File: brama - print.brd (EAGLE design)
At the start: 127.5 x 209.5 mm, 125 parts, among them IC1 AT90USB162A, IC3 AT90USB162A, J1 AVR_SPI_PRG_6OFFSET_PADS, J2 AVR_SPI_PRG_6OFFSET_PADS

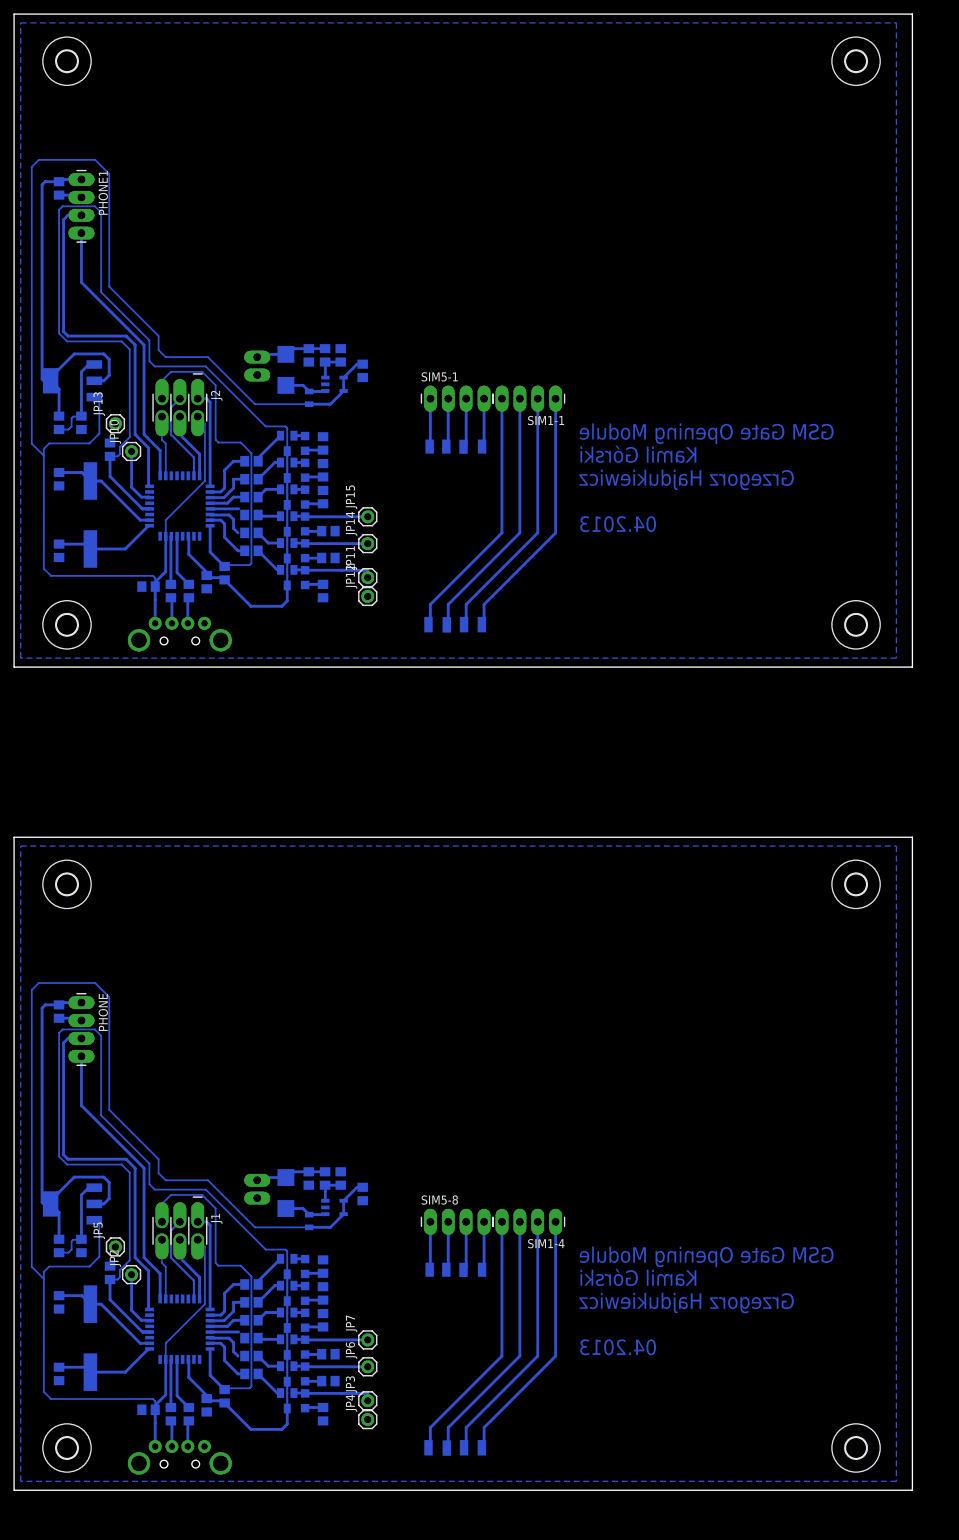
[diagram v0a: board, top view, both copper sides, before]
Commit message: L7805 Added
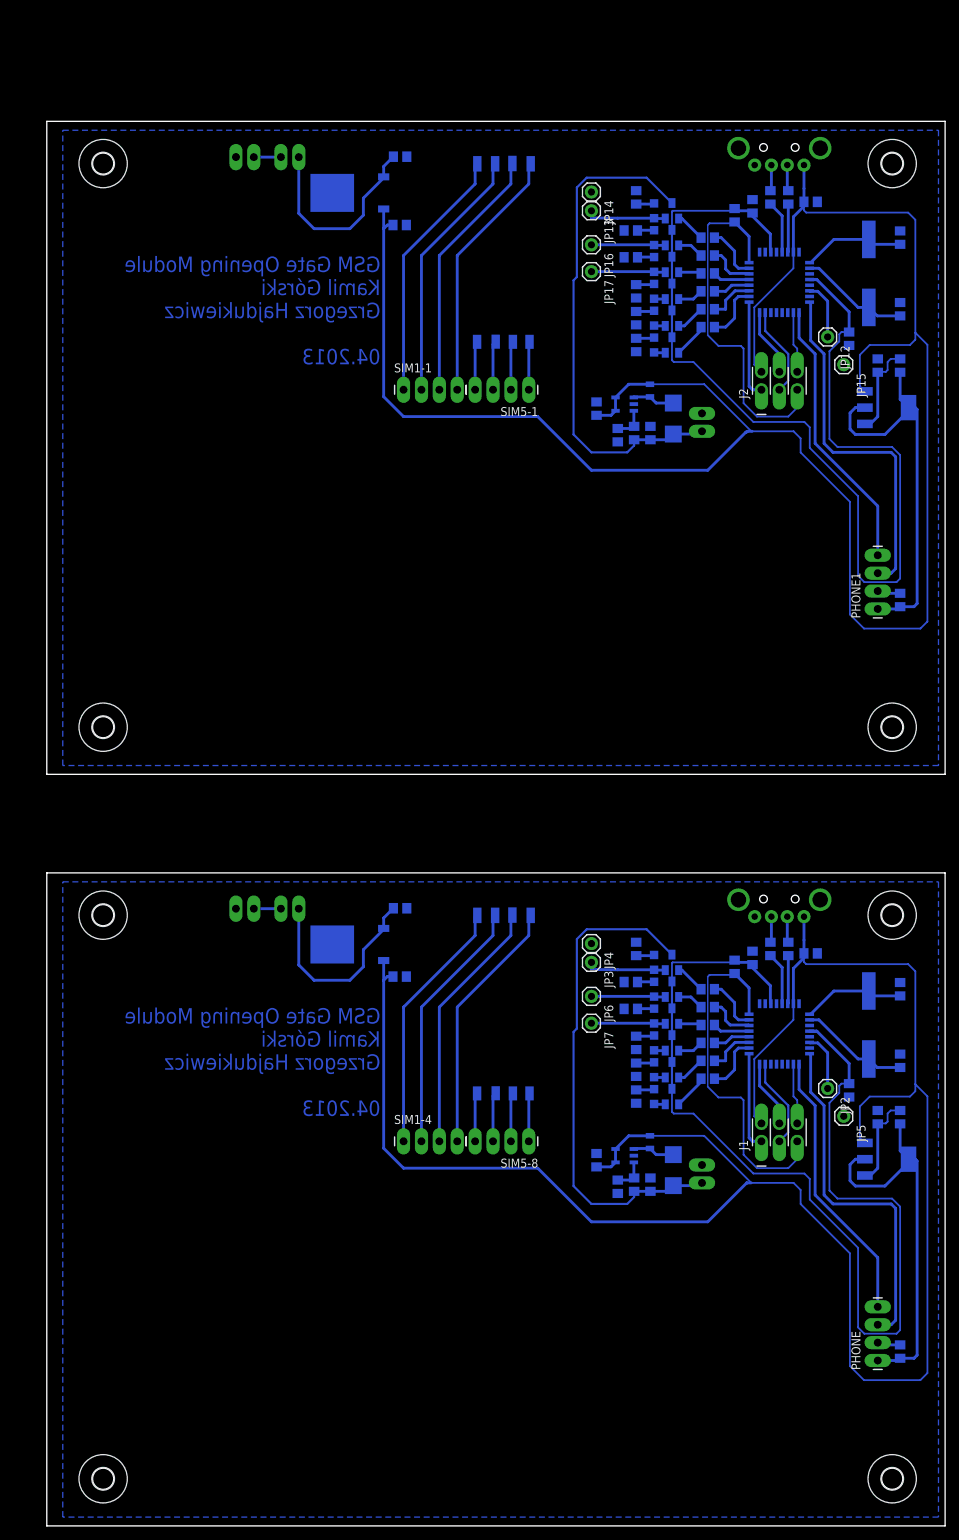
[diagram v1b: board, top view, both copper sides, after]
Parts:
- added C17, C18: 4,7uF, rcl:C0805
- added C19: 330n, rcl:C0805
- added C20: 100n, rcl:C0805
- added IC5: (no value), SparkFun-PowerIC:SOT223
- added IC6: 7806DT, linear:TO252
- added JP17: M01PTH, SparkFun-Connectors:1X01
- added JP18, JP19, JP20: (no value), SparkFun-Connectors:1X02_LONGPADS
- C10: value 22p -> 100n
- C11: value 22p -> 1uF
- C12: value 10u -> 22p
- C13: value 100n -> 22p
- C14: value 100n -> 10u
- C15, C16: value 4,7uF -> 100n
- C9: value 1uF -> 330n
- IC3: value AT90USB162A -> 7806DT; device adafruit:TQFP32-08 -> linear:TO252
- IC4: value (none) -> AT90USB162A; device SparkFun-PowerIC:SOT223 -> adafruit:TQFP32-08
- JP10: value M01PTH -> (none); device SparkFun-Connectors:1X01 -> SparkFun-Connectors:1X02_LONGPADS
- JP11: value M01PTH -> USB-A-H; device SparkFun-Connectors:1X01 -> SparkFun-Connectors:USB-A-H
- JP16: value (none) -> M01PTH; device SparkFun-Connectors:1X02_LONGPADS -> SparkFun-Connectors:1X01
- JP9: value USB-A-H -> (none); device SparkFun-Connectors:USB-A-H -> SparkFun-Connectors:1X02_LONGPADS
- R15, R34: value 100 -> 470
- moved U$10 150.5 mm to (149.4, 133.7), turned to 270 degrees
- moved U$4 144.4 mm to (149.4, 27.0), turned to 270 degrees
- moved U$8 142.7 mm to (37.4, 133.7), turned to 270 degrees
- moved U$3 139.4 mm to (149.4, 107.0), turned to 270 degrees
- moved U$2 136.2 mm to (37.4, 27.0), turned to 270 degrees
- moved U$9 134.2 mm to (149.4, 213.7), turned to 270 degrees
- moved C2 131.3 mm to (150.5, 96.5), turned to 90 degrees
- moved U$5 130.9 mm to (37.4, 107.0), turned to 270 degrees
- moved C6 128.8 mm to (150.5, 45.1), turned to 90 degrees
- moved PHONE1 128.4 mm to (147.3, 150.5), turned to 90 degrees
- moved U$11 125.3 mm to (37.4, 213.7), turned to 270 degrees
- moved C3 124.2 mm to (150.5, 86.4), turned to 90 degrees
- moved PHONE 123.9 mm to (147.3, 43.8), turned to 90 degrees
- moved R16 120.8 mm to (150.5, 78.4), turned to 270 degrees
- moved R35 119.7 mm to (150.5, 185.0), turned to 270 degrees
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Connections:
- new net VIN: C9.1, IC3.1, JP10.1
- new net VIN1: C19.1, IC6.1, JP20.1
- new net VIN_S: JP10.2, JP9.2
- new net VIN_S1: JP19.2, JP20.2
- net 12V: now also Q6.3
- net 12V1: now also C18.1, JP18.1, Q12.3; no longer C16.1, JP16.1
- net 3V1: now also C11.2, C15.1, IC4.27, IC4.4; no longer C13.1, C9.2, IC3.27, IC3.4, Q12.3
- net 3V3: no longer Q6.3
- net 5V: now also C10.1, IC3.2
- net 5V1: now also C14.1, C17.1, C20.1, IC4.31, IC5.3, IC6.2, JP11.VBUS; no longer C12.1, C15.1, IC3.31, IC4.3, JP9.VBUS
- net BUTTON3: now also IC4.6, JP12.1; no longer IC3.6, JP10.1
- net BUTTON4: now also IC4.21; no longer IC3.21
- net BUTTON5: now also IC4.22; no longer IC3.22
- net D+1: now also JP11.D+; no longer JP9.D+
- net D-1: now also JP11.D-; no longer JP9.D-
- net GATE1: now also IC4.23; no longer IC3.23
- net GND: now also C10.2, C9.2, IC3.3, JP9.1
- net GND1: now also C11.1, C17.2, C18.2, C19.2, C20.2, IC4.10, IC4.28, IC4.3, IC6.3, JP11.GND, JP14.1, JP15.1, JP18.2, JP19.1; no longer C10.2, C11.2, C9.1, IC3.10, IC3.28, IC3.3, JP12.1, JP13.1, JP16.2, JP9.GND
- net LED4: now also IC4.18; no longer IC3.18
- net LED5: now also IC4.19; no longer IC3.19
- net LED6: now also IC4.20; no longer IC3.20
- net MISO1: now also IC4.17; no longer IC3.17
- net MOSI1: now also IC4.16; no longer IC3.16
- net N$33: now also IC4.30; no longer IC3.30
- net N$35: now also IC4.29; no longer IC3.29
- net N$36: now also C13.1, IC4.2; no longer C11.1, IC3.2
- net N$40: now also JP17.1; no longer JP15.1
- net N$41: now also JP16.1; no longer JP14.1
- net N$42: now also JP13.1; no longer JP11.1
- net N$55: now also C12.1, IC4.1; no longer C10.1, IC3.1
- net N$64: now also IC5.1; no longer IC4.1
- net PHONE_PWR1: now also C16.1, IC5.2, IC5.4; no longer C14.1, IC4.2, IC4.4
- net RESET1: now also IC4.24; no longer IC3.24
- net RXD1: now also IC4.8; no longer IC3.8
- net SCK1: now also IC4.15; no longer IC3.15
- net TXD1: now also IC4.9; no longer IC3.9
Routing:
- net 5V1: track 199.0 -> 285.6 mm
- net 5V: track 199.0 -> 285.4 mm
- net 12V1: track 10.8 -> 72.5 mm
- net 12V: track 10.8 -> 72.5 mm
- net VIN1: track 0.00 -> 29.0 mm
- net VIN: track 0.00 -> 29.0 mm
- net 3V1: track 155.6 -> 150.5 mm
- net 3V3: track 155.6 -> 150.5 mm
- net VIN_S1: track 0.00 -> 3.84 mm
- net VIN_S: track 0.00 -> 3.84 mm
- net BUTTON4: track 4.05 -> 5.28 mm
- net BUTTON1: track 4.05 -> 5.28 mm
- net BUTTON2: track 5.79 -> 6.74 mm
- net BUTTON5: track 5.79 -> 6.74 mm
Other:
- board size 127.5 x 209.5 mm -> 127.5 x 199.4 mm

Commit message: nowy druk
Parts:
- added R39: 27k, rcl:R0805
- added R40: 0, rcl:R0805
- C14: value 10u -> 100n
- C16: value 100n -> 4,7uF
- C18: value 4,7uF -> 330n
- C19: value 330n -> 100n
- C20: value 100n -> 22p
- C4: value 10u -> 22p
- E$1: device frames:A4-35SCP -> frames:A4P-LOC
- JP1, JP11: value USB-A-H -> USBSMD; device SparkFun-Connectors:USB-A-H -> SparkFun-Connectors:USB-MINIB
- R20: value 22R -> 0
- R22: value 4k7 -> 22R
- R23: value (none) -> 4k7
- R29: value 100 -> (none)
- R34: value 470 -> 100
- R35: value (none) -> 470
- R37: value 240k -> (none)
- R38: value 27k -> 240k
- moved U$9 267.0 mm to (-100.7, 120.2), turned to 0 degrees
- moved R35 266.4 mm to (-95.9, 83.8), turned to 180 degrees
- moved JP11 261.3 mm to (-102.9, 104.1), turned to 180 degrees
- moved C12 254.2 mm to (-90.2, 121.3), turned to 0 degrees
- moved R21 252.2 mm to (-96.6, 102.5), turned to 180 degrees
- moved C18 250.3 mm to (-101.7, 50.3)
- moved C11 248.7 mm to (-94.6, 99.8), turned to 180 degrees
- moved U$7 248.4 mm to (-101.6, 73.7), turned to 180 degrees
- moved U$11 247.6 mm to (-100.7, 8.16), turned to 0 degrees
- moved JP19 245.2 mm to (-101.6, 27.0), turned to 90 degrees
- moved Y2 245.0 mm to (-85.1, 116.8), turned to 0 degrees
- moved R22 244.8 mm to (-95.6, 104.5), turned to 180 degrees
- moved JP20 244.4 mm to (-101.6, 35.9), turned to 270 degrees
- moved Q12 242.8 mm to (-94.0, 88.9), turned to 270 degrees
- moved JP14 242.5 mm to (-96.6, 77.5), turned to 0 degrees
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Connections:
- net 12V1: now also C17.1, R38.2; no longer C18.1, R37.2
- net 3V1: now also C14.1, R23.2; no longer C15.1, R22.2
- net 5V: now also C4.2; no longer C4.1
- net 5V1: now also C16.1, C19.1, C20.2; no longer C14.1, C17.1, C20.1
- net BUTTON4: now also R27.2; no longer R26.2
- net BUTTON5: now also R28.2; no longer R27.2
- net D+1: now also R22.1; no longer R21.1
- net D-1: now also R21.1; no longer R20.1
- net GATE1: now also R29.2; no longer R28.2
- net GND: now also C4.1, R20.1, R20.2; no longer C4.2
- net GND1: now also C20.1, R35.1, R37.1, R39.1, R40.1, R40.2; no longer C20.2, R29.1, R36.1, R38.1
- net LED4: now also R24.2; no longer R23.2
- net LED5: now also R25.2; no longer R24.2
- net LED6: now also R26.2; no longer R25.2
- net N$33: now also R21.2; no longer R20.2
- net N$35: now also R22.2; no longer R21.2
- net N$43: now also R24.1; no longer R23.1
- net N$44: now also R25.1; no longer R24.1
- net N$45: now also R26.1; no longer R25.1
- net N$46: now also R27.1; no longer R26.1
- net N$47: now also R28.1; no longer R27.1
- net N$48: now also R29.1; no longer R28.1
- net N$49: now also R30.2; no longer R29.2
- net N$50: now also R31.2; no longer R30.2
- net N$51: now also R32.2; no longer R31.2
- net N$52: now also R33.2; no longer R32.2
- net N$53: now also R34.2; no longer R33.2
- net N$54: now also R35.2; no longer R34.2
- net N$64: now also R36.1, R37.2; no longer R35.1, R36.2
- net N$65: now also R38.1, R39.2; no longer R37.1, R38.2
- net PHONE_PWR1: now also C15.1, R36.2; no longer C16.1, R35.2
- net RESET1: now also R23.1; no longer R22.1
- net VIN1: now also C18.1; no longer C19.1
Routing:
- net 5V: track 285.4 -> 314.5 mm
- net 5V1: track 285.6 -> 314.5 mm
- net VIN1: track 29.0 -> 17.0 mm
- net VIN: track 29.0 -> 17.0 mm
- net N$1: track 6.85 -> 11.5 mm
- net N$33: track 6.85 -> 11.5 mm
- net N$35: track 7.51 -> 6.53 mm
- net N$2: track 7.51 -> 6.53 mm
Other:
- board size 127.5 x 199.4 mm -> 199.4 x 127.5 mm

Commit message: piszemy soft
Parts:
- removed C12, C13, C20: 22p, rcl:C0805
- removed C14, C15, C19: 100n, rcl:C0805
- removed C16, C17: 4,7uF, rcl:C0805
- removed C18: 330n, rcl:C0805
- removed D2: (no value), SparkFun-DiscreteSemi:SMB-DIODE
- removed E$1: (no value), frames:A4P-LOC
- removed IC5: (no value), SparkFun-PowerIC:SOT223
- removed IC6: 7806DT, linear:TO252
- removed J1, J2: AVR_SPI_PRG_6OFFSET_PADS, SparkFun-Connectors:2X3_OFFSET
- removed JP11: USBSMD, SparkFun-Connectors:USB-MINIB
- removed JP12, JP13, JP14, JP15, JP16, JP17: M01PTH, SparkFun-Connectors:1X01
- removed JP18, JP19, JP20: (no value), SparkFun-Connectors:1X02_LONGPADS
- removed L2: (no value), SparkFun-Passives:0805
- removed LED10, LED11, LED12, LED7, LED8, LED9: (no value), led:CHIPLED_0805
- removed PHONE1, SIM1-1, SIM5-1: (no value), SparkFun-Connectors:1X04_LONGPADS
- removed Q10, Q11, Q12, Q7, Q8, Q9: (no value), SparkFun-DiscreteSemi:SOT23
- removed R23: 4k7, rcl:R0805
- removed R24, R25, R26, R27, R28, R29, R36, R37: (no value), rcl:R0805
- removed R30, R31, R32, R33, R34: 100, rcl:R0805
- removed R35: 470, rcl:R0805
- removed R38: 240k, rcl:R0805
- removed R39: 27k, rcl:R0805
- removed R40: 0, rcl:R0805
- removed U$10, U$11, U$8, U$9: (no value), holes:3,0
- removed U$12: LM2704MF-ADJ, Step-Up:SOT23-5
- removed U$7: SIMHOLDER2, SparkFun-Connectors:SIMHOLDER2
- removed Y2: (no value), SparkFun-FreqCtrl:HC49UP
- C11: value 1uF -> 100n
- IC4: value AT90USB162A -> (none); device adafruit:TQFP32-08 -> SparkFun-PowerIC:SOT223
- R21, R22: value 22R -> (none)
- moved R22 123.4 mm to (12.7, 45.4), turned to 0 degrees
- moved R21 122.1 mm to (13.5, 49.7), turned to 90 degrees
- moved IC4 104.9 mm to (6.21, 50.3), turned to 90 degrees
- moved C11 104.1 mm to (9.40, 96.8), turned to 0 degrees
- moved C5 34.5 mm to (35.3, 79.9), turned to 270 degrees
- moved C7 24.6 mm to (32.2, 101.2), turned to 90 degrees
- moved U$6 20.0 mm to (36.2, 101.8), turned to 270 degrees
- moved R19 18.7 mm to (35.2, 97.4), turned to 90 degrees
- moved L1 18.1 mm to (39.8, 103.8), turned to 270 degrees
- moved R20 16.2 mm to (3.81, 96.7), turned to 0 degrees
- moved R18 15.7 mm to (37.6, 97.7), turned to 270 degrees
- moved C8 12.7 mm to (39.9, 97.7), turned to 90 degrees
- moved C10 12.5 mm to (10.4, 39.0)
- moved C9 12.5 mm to (4.53, 37.8)
- moved IC3 12.5 mm to (9.67, 30.7)
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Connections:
- removed net 12V1: C17.1, D2.C, JP18.1, Q12.3, R38.2
- removed net 3V1: C11.2, C14.1, IC4.27, IC4.4, Q10.3, Q11.3, Q7.3, Q8.3, Q9.3, R23.2
- removed net 5V1: C16.1, C19.1, C20.2, IC4.31, IC5.3, IC6.2, J2.2, JP11.VBUS, L2.1, U$12.!SHDN, U$12.VIN
- removed net BUTTON3: IC4.6, JP12.1
- removed net BUTTON4: IC4.21, R27.2
- removed net BUTTON5: IC4.22, R28.2
- removed net D+1: JP11.D+, R22.1
- removed net D-1: JP11.D-, R21.1
- removed net GATE1: IC4.23, R29.2
- removed net GND1: C11.1, C12.2, C13.2, C14.2, C15.2, C16.2, C17.2, C18.2, C19.2, C20.1, IC4.10, IC4.28, IC4.3, IC6.3, J2.6, JP11.GND, JP14.1, JP15.1, JP18.2, JP19.1, PHONE1.2, R30.1, R31.1, R32.1, R33.1, R34.1, R35.1, R37.1, R39.1, R40.1, R40.2, U$12.GND
- removed net LED4: IC4.18, R24.2
- removed net LED5: IC4.19, R25.2
- removed net LED6: IC4.20, R26.2
- removed net MISO: IC1.17, J1.1
- removed net MISO1: IC4.17, J2.1
- removed net MOSI: IC1.16, J1.4
- removed net MOSI1: IC4.16, J2.4
- removed net N$35: IC4.29, R22.2
- removed net N$36: C13.1, IC4.2, Y2.1
- removed net N$37: LED7.A, Q7.2
- removed net N$38: LED8.A, Q8.2
- removed net N$39: LED9.A, Q9.2
- removed net N$40: JP17.1, LED10.A, Q10.2
- removed net N$41: JP16.1, LED11.A, Q11.2
- removed net N$42: JP13.1, LED12.A, Q12.2
- removed net N$43: Q7.1, R24.1
- removed net N$44: Q8.1, R25.1
- removed net N$45: Q9.1, R26.1
- removed net N$46: Q10.1, R27.1
- removed net N$47: Q11.1, R28.1
- removed net N$48: Q12.1, R29.1
- removed net N$49: LED7.C, R30.2
- removed net N$50: LED8.C, R31.2
- removed net N$51: LED9.C, R32.2
- removed net N$52: LED10.C, R33.2
- removed net N$53: LED11.C, R34.2
- removed net N$54: LED12.C, R35.2
- removed net N$55: C12.1, IC4.1, Y2.2
- removed net N$56: SIM1-1.4, U$7.1
- removed net N$57: SIM5-1.1, U$7.8
- removed net N$58: SIM5-1.2, U$7.7
- removed net N$59: SIM5-1.3, U$7.6
- removed net N$60: SIM5-1.4, U$7.5
- removed net N$61: SIM1-1.1, U$7.4
- removed net N$62: SIM1-1.2, U$7.3
- removed net N$63: SIM1-1.3, U$7.2
- removed net N$64: IC5.1, R36.1, R37.2
- removed net N$65: R38.1, R39.2, U$12.FB
- removed net N$66: D2.A, L2.2, U$12.SW
- removed net PHONE_PWR1: C15.1, IC5.2, IC5.4, PHONE1.1, R36.2
- removed net RESET1: IC4.24, J2.5, R23.1
- removed net RXD1: IC4.8, PHONE1.3
- removed net SCK: IC1.15, J1.3
- removed net SCK1: IC4.15, J2.3
- removed net TXD1: IC4.9, PHONE1.4
- removed net VIN1: C18.1, IC6.1, JP20.1
- removed net VIN_S1: JP19.2, JP20.2
- new net UCAP: C1.2, IC1.27
- net 3V3: now also C11.1, IC1.32, IC4.2, IC4.4, R21.2; no longer C1.2, IC1.27
- net 5V: now also IC4.3; no longer J1.2
- net GND: now also C11.2, R22.1; no longer IC1.10, J1.6
- net N$33: now also IC4.1, R21.1, R22.2; no longer IC4.30, R21.2
- net RESET: no longer J1.5
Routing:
- net 5V1: track 314.5 -> 0.00 mm
- net 3V1: track 150.6 -> 0.00 mm
- net 12V1: track 72.2 -> 0.00 mm
- net RESET1: track 57.4 -> 0.00 mm
- net PHONE_PWR1: track 55.7 -> 0.00 mm
- net RXD1: track 50.5 -> 0.00 mm
- net RESET: track 57.4 -> 8.89 mm
- net 5V: track 314.5 -> 357.2 mm
- net TXD1: track 39.1 -> 0.00 mm
- net N$61: track 36.4 -> 0.00 mm
- net N$63: track 36.4 -> 0.00 mm
- net N$62: track 36.4 -> 0.00 mm
- net N$56: track 36.4 -> 0.00 mm
- net 3V3: track 150.6 -> 124.0 mm
- net VIN1: track 17.0 -> 0.00 mm
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- removed copper zone on layer 16, net GND1
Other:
- board size 199.4 x 127.5 mm -> 95 x 127.5 mm
